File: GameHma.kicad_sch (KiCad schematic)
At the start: 10 parts, among them J1 Screw_Terminal_01x02, J2 Motor_Terminal_01x06, J3 Motor_Terminal_01x06, J4 Motor_Terminal_01x06, J5 Motor_Terminal_01x06, U1 ESP32-DEVKIT-V1, U2 A4988_STEPPER_MOTOR_DRIVER_CA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, U3 A4988_STEPPER_MOTOR_DRIVER_CA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, U4 A4988_STEPPER_MOTOR_DRIVER_CA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, U5 A4988_STEPPER_MOTOR_DRIVER_CA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

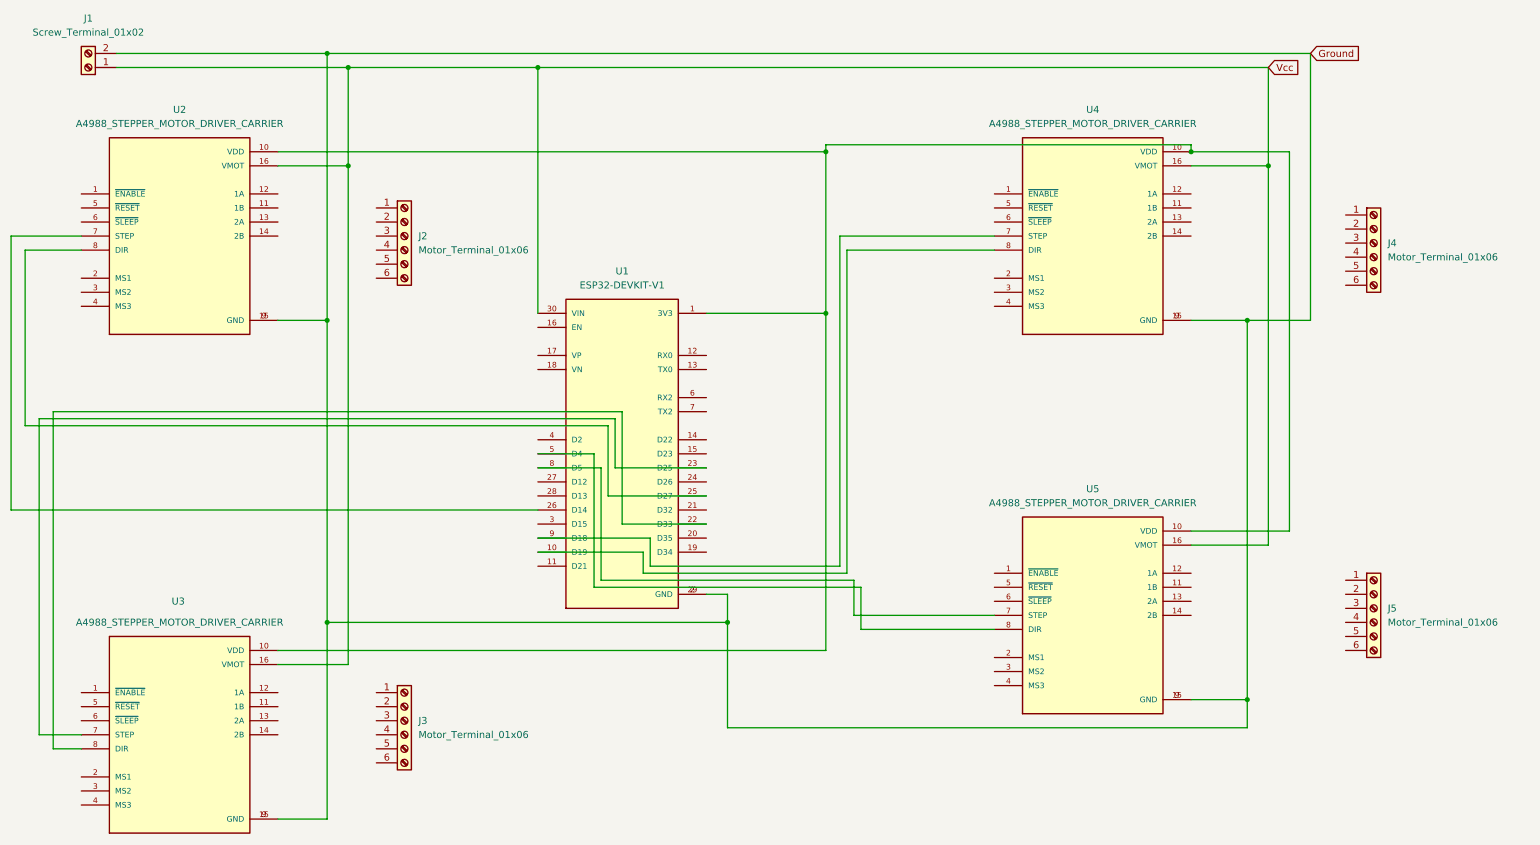
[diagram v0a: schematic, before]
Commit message: delete terminal motor, jump wires SLEEP and RESET together(Cyan)
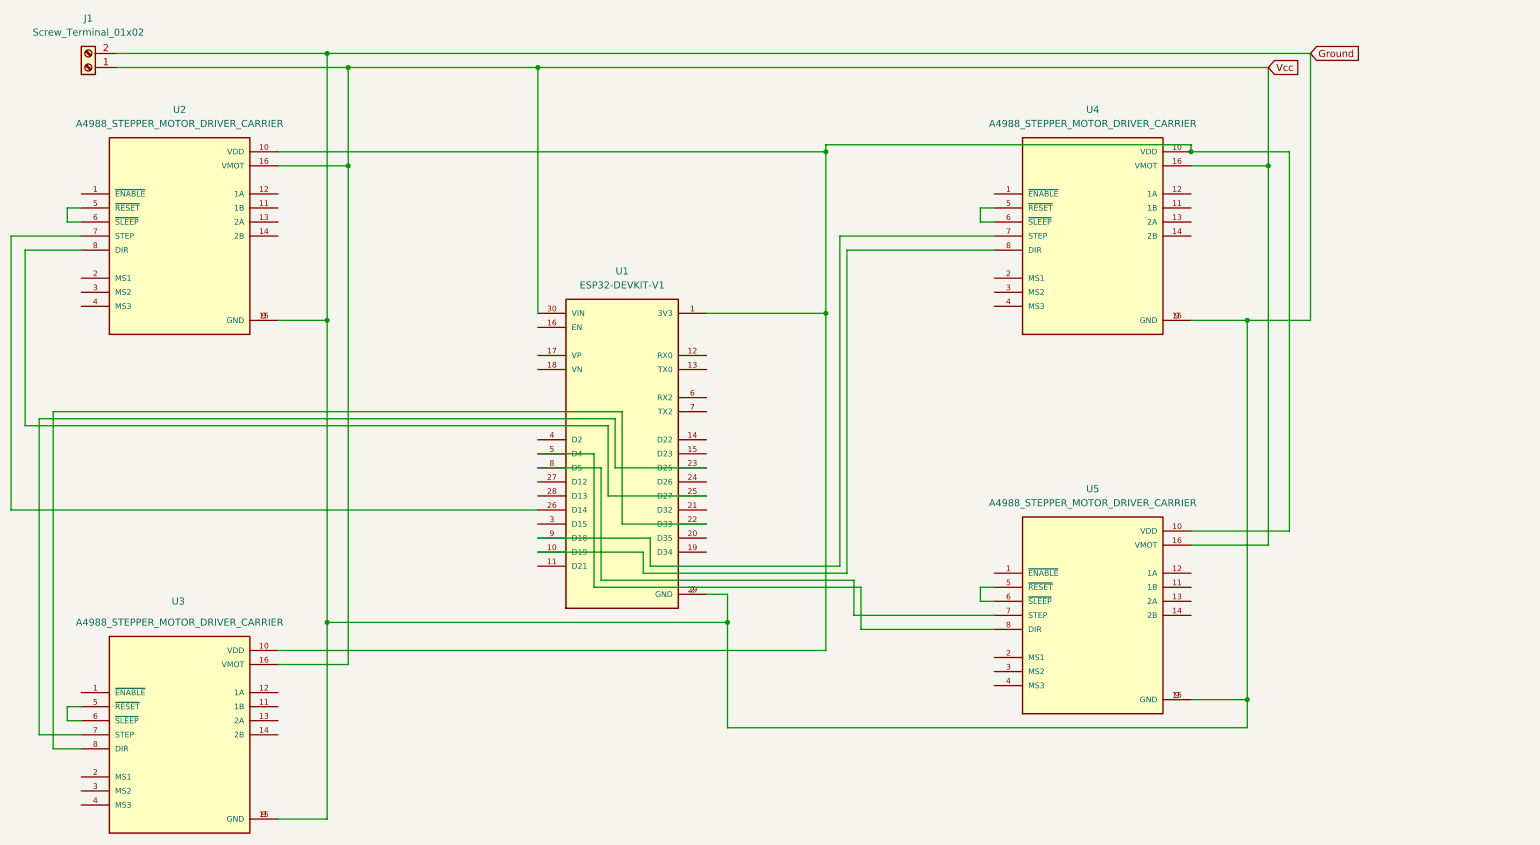
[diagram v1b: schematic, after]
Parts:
- removed J2, J3, J4, J5: Motor_Terminal_01x06, symbol Connector:Screw_Terminal_01x06
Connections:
- net at U2.5 (~{RESET}): now also U2.6 (~{SLEEP})
- net at U3.5 (~{RESET}): now also U3.6 (~{SLEEP})
- net at U5.5 (~{RESET}): now also U5.6 (~{SLEEP})
- net at U4.5 (~{RESET}): now also U4.6 (~{SLEEP})

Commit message: add new motor termina(1x4) then connected wires to it
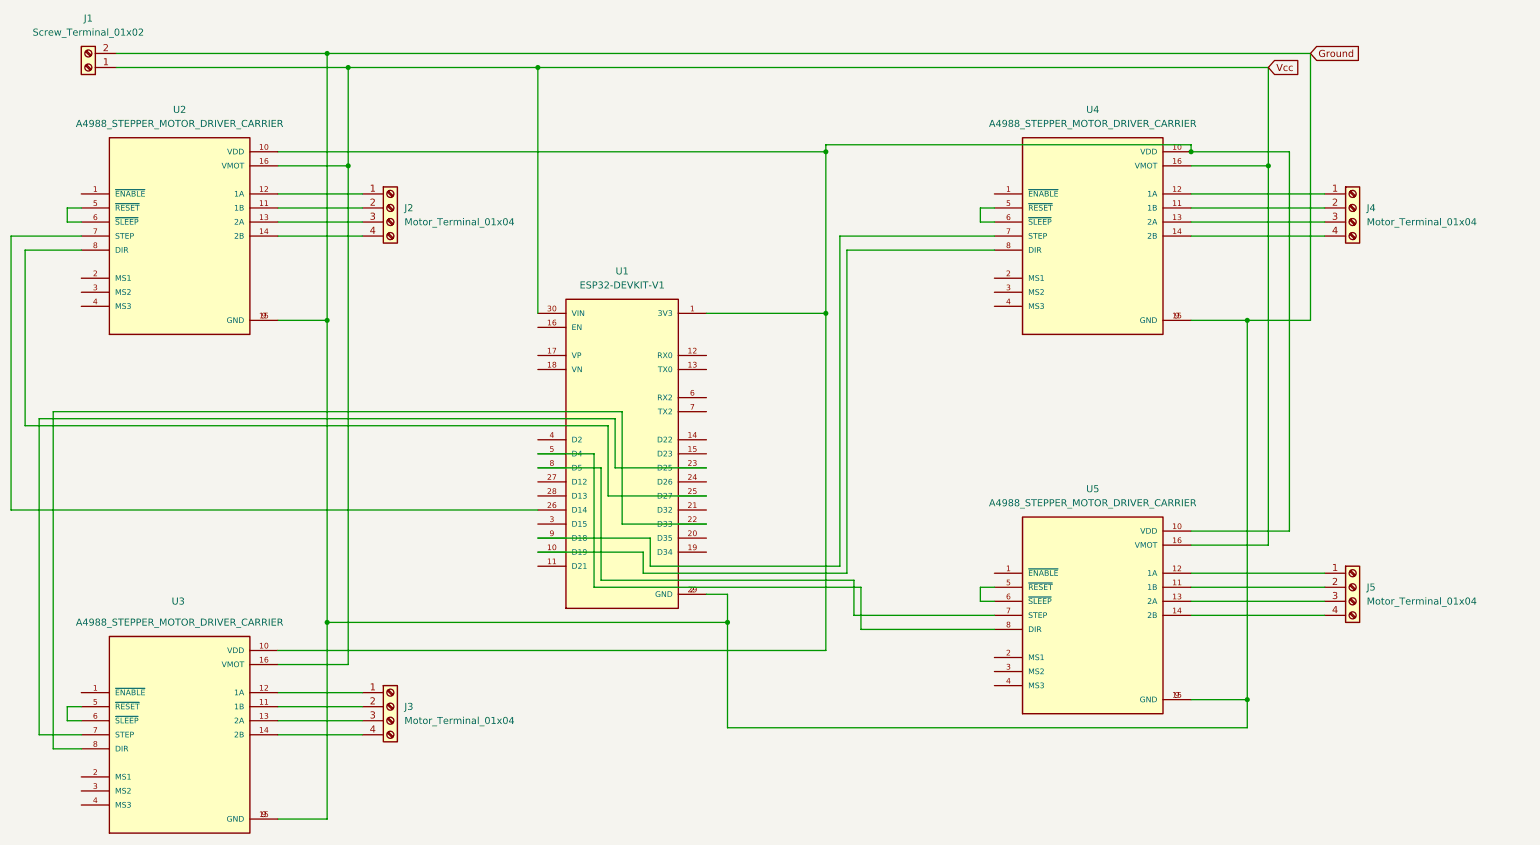
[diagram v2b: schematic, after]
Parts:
- added J2, J3, J4, J5: Motor_Terminal_01x04, symbol Connector:Screw_Terminal_01x04
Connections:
- net at U2.11 (1B): now also J2.2 (Pin_2)
- net at U2.12 (1A): now also J2.1 (Pin_1)
- net at U2.13 (2A): now also J2.3 (Pin_3)
- net at U2.14 (2B): now also J2.4 (Pin_4)
- net at U3.11 (1B): now also J3.2 (Pin_2)
- net at U3.12 (1A): now also J3.1 (Pin_1)
- net at U3.13 (2A): now also J3.3 (Pin_3)
- net at U3.14 (2B): now also J3.4 (Pin_4)
- net at U5.11 (1B): now also J5.2 (Pin_2)
- net at U5.12 (1A): now also J5.1 (Pin_1)
- net at U5.13 (2A): now also J5.3 (Pin_3)
- net at U5.14 (2B): now also J5.4 (Pin_4)
- net at U4.11 (1B): now also J4.2 (Pin_2)
- net at U4.12 (1A): now also J4.1 (Pin_1)
- net at U4.13 (2A): now also J4.3 (Pin_3)
- net at U4.14 (2B): now also J4.4 (Pin_4)

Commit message: edit wires color of moters
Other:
- company: (none) -> OpenFruit
- title: (none) -> PineappleBoard
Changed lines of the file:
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@@
 	(paper "A4")
 	(title_block
+		(title "PineappleBoard")
 		(date "2025-08-07")
 		(rev "0")
+		(company "OpenFruit")
 	)
 	(junction
@@
 			(width 0)
 			(type default)
+			(color 255 0 0 1)
 		)
 	)
@@
 			(width 0)
 			(type default)
+			(color 0 0 194 1)
 		)
 	)
@@
 			(width 0)
 			(type default)
+			(color 255 0 255 1)
 		)
 	)
@@
 			(width 0)
 			(type default)
+			(color 72 72 72 1)
 		)
 	)
@@
 			(width 0)
 			(type default)
+			(color 255 0 255 1)
 		)
 	)
@@
 			(width 0)
 			(type default)
+			(color 255 0 255 1)
 		)
 	)
@@
 			(width 0)
 			(type default)
+			(color 72 72 72 1)
 		)
 	)
@@
 			(width 0)
 			(type default)
+			(color 72 72 72 1)
 		)
 	)
@@
 			(width 0)
 			(type default)
+			(color 72 72 72 1)
 		)
 	)
@@
 			(width 0)
 			(type default)
+			(color 255 0 0 1)
 		)
 	)
@@
 			(width 0)
 			(type default)
+			(color 0 0 194 1)
 		)
 	)
@@
 			(width 0)
 			(type default)
+			(color 255 0 0 1)
 		)
 	)
@@
 			(width 0)
 			(type default)
+			(color 255 0 0 1)
 		)
 	)
@@
 			(width 0)
 			(type default)
+			(color 255 0 255 1)
 		)
 	)
@@
 			(width 0)
 			(type default)
+			(color 0 0 194 1)
 		)
 	)
@@
 			(width 0)
 			(type default)
-		)
-	)
+			(color 0 0 194 1)
+		)
+	)

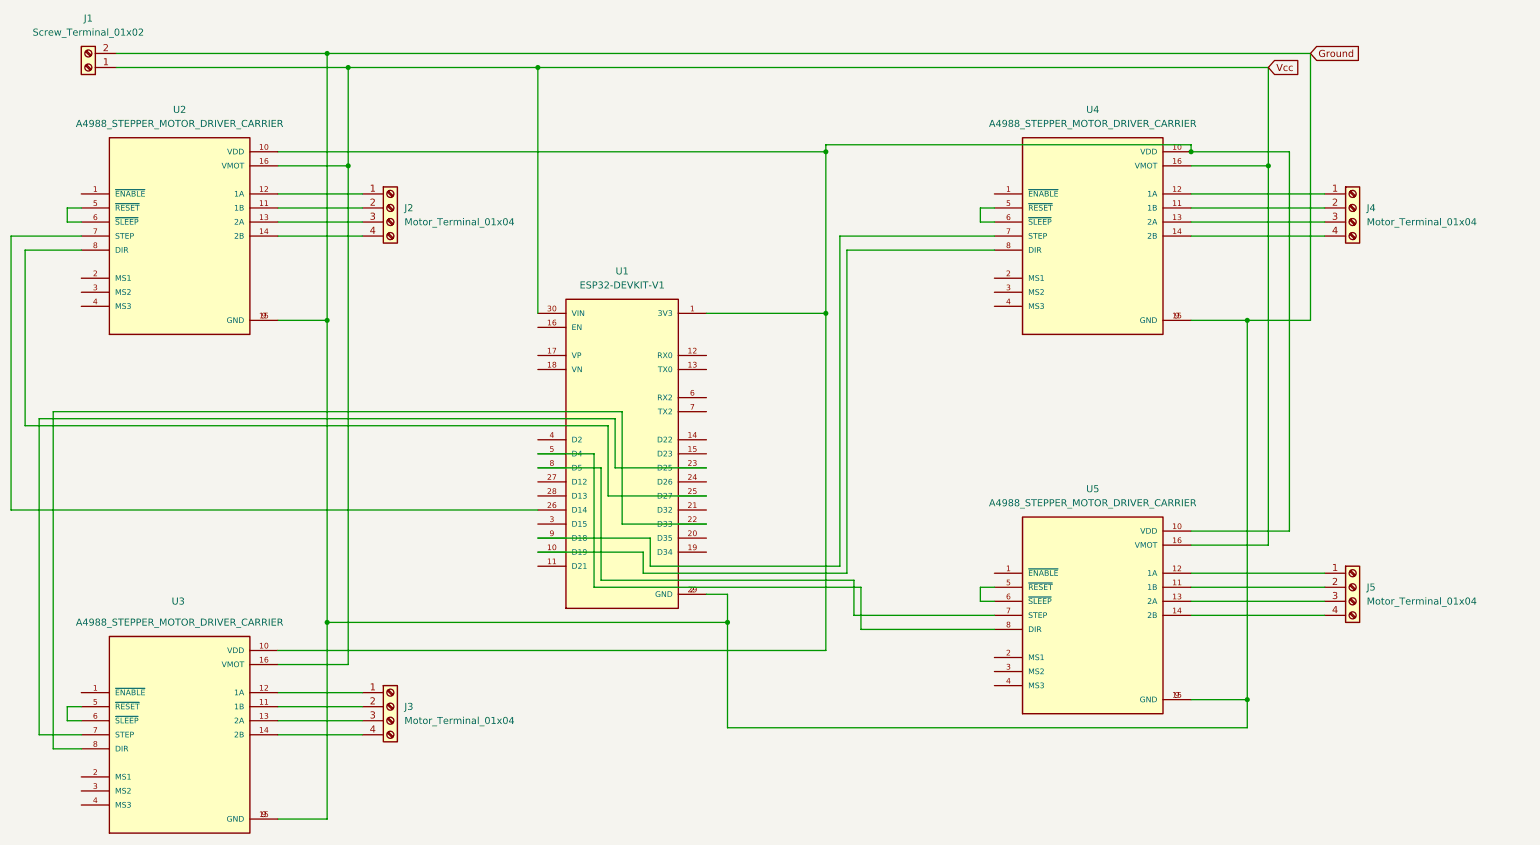
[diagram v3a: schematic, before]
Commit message: edit motor terminal wires
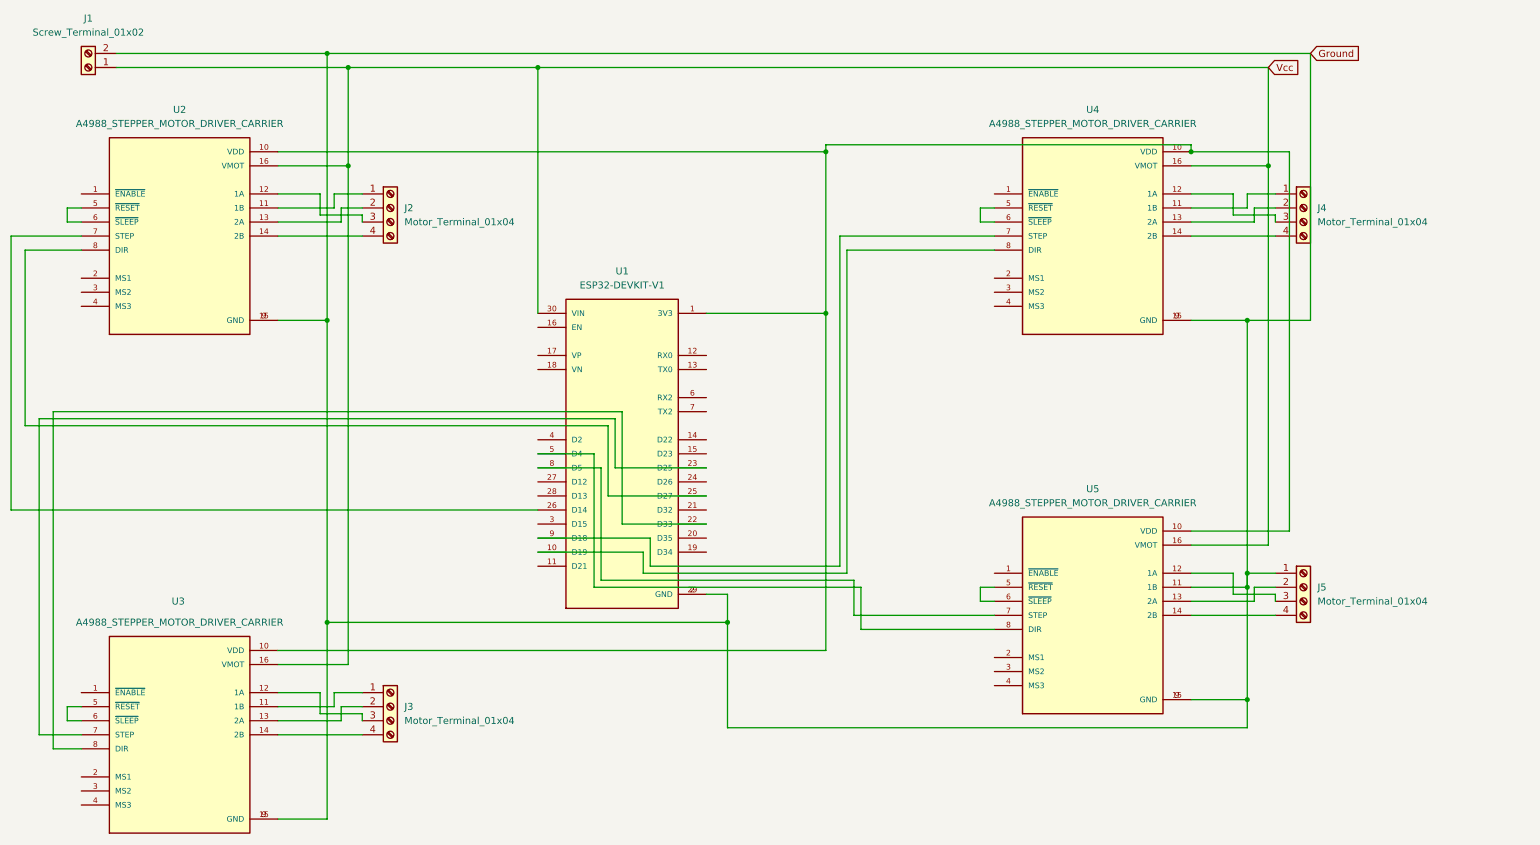
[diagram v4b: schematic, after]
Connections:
- net Ground: now also J5.1 (Pin_1), U5.11 (1B)
- net at J2.1 (Pin_1): now also U2.11 (1B); no longer U2.12 (1A)
- net at J2.2 (Pin_2): now also U2.13 (2A); no longer U2.11 (1B)
- net at J2.3 (Pin_3): now also U2.12 (1A); no longer U2.13 (2A)
- net at J3.1 (Pin_1): now also U3.11 (1B); no longer U3.12 (1A)
- net at J3.2 (Pin_2): now also U3.13 (2A); no longer U3.11 (1B)
- net at J3.3 (Pin_3): now also U3.12 (1A); no longer U3.13 (2A)
- net at J5.2 (Pin_2): now also U5.13 (2A); no longer U5.11 (1B)
- net at U5.12 (1A): now also J5.3 (Pin_3); no longer J5.1 (Pin_1)
- net at J4.1 (Pin_1): now also U4.11 (1B); no longer U4.12 (1A)
- net at J4.2 (Pin_2): now also U4.13 (2A); no longer U4.11 (1B)
- net at J4.3 (Pin_3): now also U4.12 (1A); no longer U4.13 (2A)

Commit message: fix wire error, add capcitor 100u to each a4988
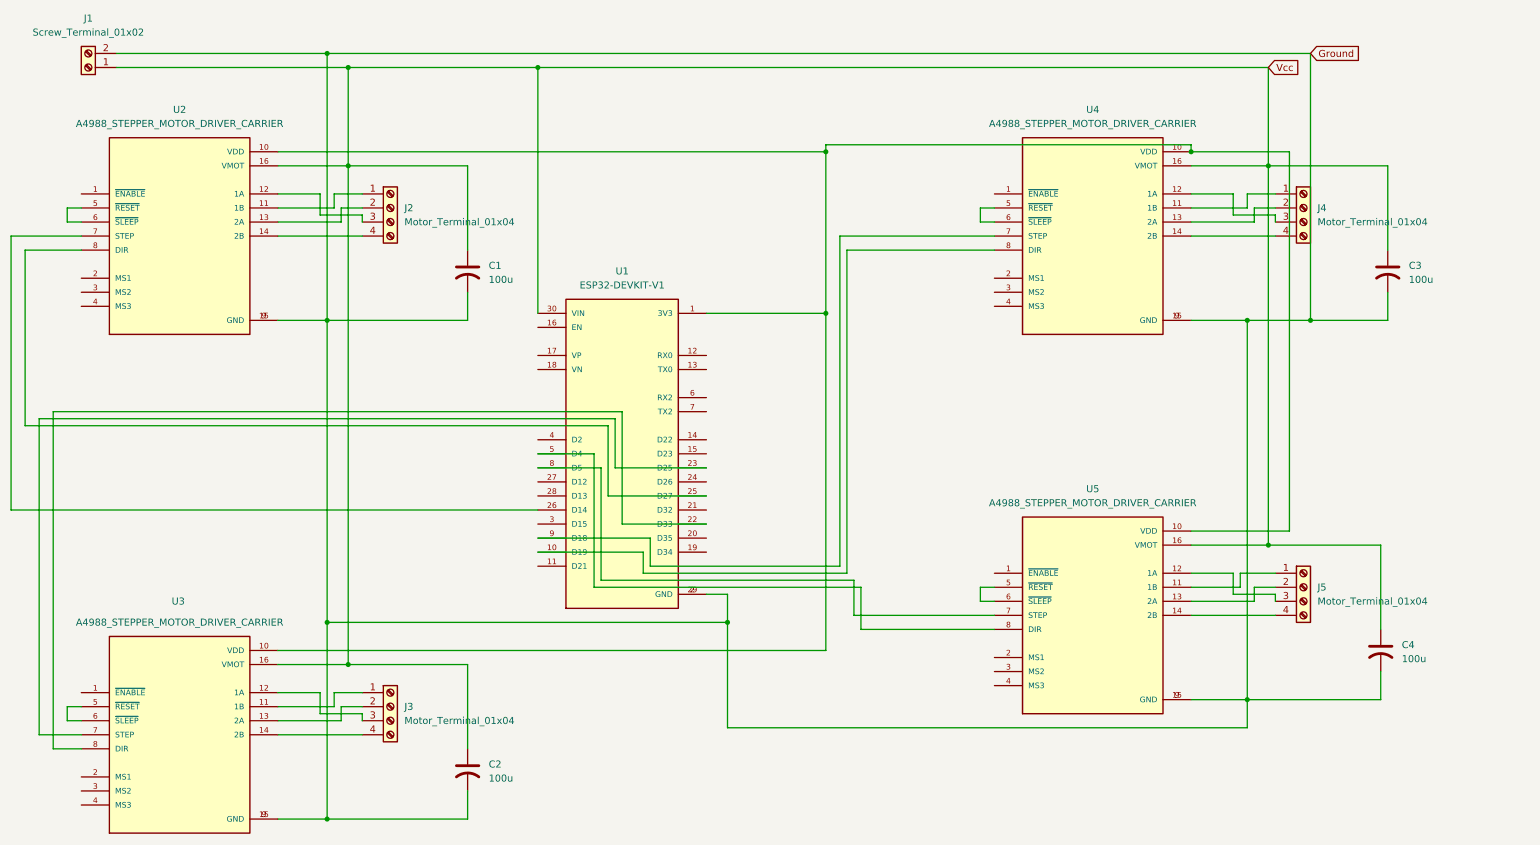
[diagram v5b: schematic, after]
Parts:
- added C1, C2, C3, C4: 100u, symbol Device:C_US
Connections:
- net Ground: now also C1.2, C2.2, C3.2, C4.2; no longer J5.1 (Pin_1), U5.11 (1B)
- net Vcc: now also C1.1, C2.1, C3.1, C4.1
- new net: J5.1 (Pin_1), U5.11 (1B)
